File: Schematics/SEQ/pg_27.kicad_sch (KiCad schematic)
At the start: 9 parts, among them U2801 F04, U2802 F169, U2803 F169, U2804 F169, U2805 F169, U2806 F169, U2807 F244, U2808 F244, U2809 F244

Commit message: Much work on SEQ
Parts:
- removed U2803, U2804, U2805, U2806: F169, symbol r1000:F169
- removed U2808, U2809: F244, symbol r1000:F244
- U2802: value F169 -> F169X5; symbol r1000:F169 -> r1000:F169X5; Location K13 -> x99; Name TOP0 -> TOPCNT
- U2807: value F244 -> XBUF20; symbol r1000:F244 -> r1000:XBUF20; Location L13 -> x99; Name RESDRV0A -> TOPDV
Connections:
- net CONTROL_BUS37: now also U2802.5 (D0); no longer U2802.6 (D0)
- net CONTROL_BUS38: now also U2802.7 (D1); no longer U2802.5 (D1)
- net CONTROL_BUS39: now also U2802.9 (D2); no longer U2802.4 (D2)
- net CONTROL_BUS40: now also U2802.11 (D3); no longer U2802.3 (D3)
- net CONTROL_BUS41: now also U2802.13 (D4)
- net CONTROL_BUS42: now also U2802.15 (D5)
- net CONTROL_BUS43: now also U2802.17 (D6)
- net CONTROL_BUS44: now also U2802.19 (D7)
- net CONTROL_BUS45: now also U2802.21 (D8)
- net CONTROL_BUS46: now also U2802.23 (D9)
- net CONTROL_BUS47: now also U2802.25 (D10)
- net CONTROL_BUS48: now also U2802.27 (D11)
- net CONTROL_BUS49: now also U2802.29 (D12)
- net CONTROL_BUS50: now also U2802.31 (D13)
- net CONTROL_BUS51: now also U2802.33 (D14)
- net CONTROL_BUS52: now also U2802.35 (D15)
- net CONTROL_BUS53: now also U2802.37 (D16)
- net CONTROL_BUS54: now also U2802.39 (D17)
- net CONTROL_BUS55: now also U2802.41 (D18)
- net CONTROL_BUS56: now also U2802.43 (D19)
- net OFFSET_BUS37: now also U2807.4 (Y0); no longer U2807.18 (Y0)
- net OFFSET_BUS38: now also U2807.6 (Y1); no longer U2807.16 (Y1)
- net OFFSET_BUS39: now also U2807.8 (Y2); no longer U2807.14 (Y2)
- net OFFSET_BUS40: now also U2807.10 (Y3); no longer U2807.12 (Y3)
- net OFFSET_BUS41: now also U2807.12 (Y4)
- net OFFSET_BUS42: now also U2807.14 (Y5)
- net OFFSET_BUS43: now also U2807.16 (Y6)
- net OFFSET_BUS44: now also U2807.18 (Y7)
- net OFFSET_BUS45: now also U2807.20 (Y8)
- net OFFSET_BUS46: now also U2807.22 (Y9)
- net OFFSET_BUS47: now also U2807.24 (Y10)
- net OFFSET_BUS48: now also U2807.26 (Y11)
- net OFFSET_BUS49: now also U2807.28 (Y12)
- net OFFSET_BUS50: now also U2807.30 (Y13)
- net OFFSET_BUS51: now also U2807.32 (Y14)
- net OFFSET_BUS52: now also U2807.34 (Y15)
- net OFFSET_BUS53: now also U2807.36 (Y16)
- net OFFSET_BUS54: now also U2807.38 (Y17)
- net OFFSET_BUS55: now also U2807.40 (Y18)
- net OFFSET_BUS56: now also U2807.42 (Y19)
- net TOP.CLK~: now also U2802.1 (CLK); no longer U2802.2 (CLK)
- net TOP.EN~: now also U2802.45 (ENP); no longer U2802.7 (ENP)
- net TOP.OE~: now also U2807.2 (OE); no longer U2807.1 (OE0)
- net TOP.U_D~: now also U2802.3 (UP); no longer U2802.1 (UP)
- net TOP37: now also U2802.6 (Q0), U2807.3 (I0); no longer U2802.11 (Q0), U2807.2 (I0)
- net TOP38: now also U2802.8 (Q1), U2807.5 (I1); no longer U2802.12 (Q1), U2807.4 (I1)
- net TOP39: now also U2802.10 (Q2), U2807.7 (I2); no longer U2802.13 (Q2), U2807.6 (I2)
- net TOP40: now also U2802.12 (Q3), U2807.9 (I3); no longer U2802.14 (Q3), U2807.8 (I3)
- net TOP41: now also U2802.14 (Q4), U2807.11 (I4)
- net TOP42: now also U2802.16 (Q5), U2807.13 (I5)
- net TOP43: now also U2802.18 (Q6), U2807.15 (I6)
- net TOP44: now also U2802.20 (Q7), U2807.17 (I7)
- net TOP45: now also U2802.22 (Q8), U2807.19 (I8)
- net TOP46: now also U2802.24 (Q9), U2807.21 (I9)
- net TOP47: now also U2802.26 (Q10), U2807.23 (I10)
- net TOP48: now also U2802.28 (Q11), U2807.25 (I11)
- net TOP49: now also U2802.30 (Q12), U2807.27 (I12)
- net TOP50: now also U2802.32 (Q13), U2807.29 (I13)
- net TOP51: now also U2802.34 (Q14), U2807.31 (I14)
- net TOP52: now also U2802.36 (Q15), U2807.33 (I15)
- net TOP53: now also U2802.38 (Q16), U2807.35 (I16)
- net TOP54: now also U2802.40 (Q17), U2807.37 (I17)
- net TOP55: now also U2802.42 (Q18), U2807.39 (I18)
- net TOP56: now also U2802.44 (Q19), U2807.41 (I19)
- net TOP_LD.RND~: now also U2802.2 (LD); no longer U2802.9 (LD)
- net at U2801.2 (Q): now also U2802.46 (ENT)
- no-connect marks 10 -> 2
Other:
- moved on the sheet: U2801

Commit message: KiCad 6
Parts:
- U2801: value F04 -> (none)
- U2802: value F169X5 -> (none)
- U2807: value XBUF20 -> (none)
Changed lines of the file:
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@@
   (wire (pts (xy 365.76 251.46) (xy 408.94 251.46) ) (stroke (width 0) (type solid) (color 0 0 0 0) ) )
   (global_label "LOCL_STOP.DIAG~" (shape input) (at 114.3 261.62 180) (fields_autoplaced) (effects (font (size 2.54 2.54) ) (justify right) ) (property "Intersheet References" "${INTERSHEET_REFS}" (id 0) (at 77.1797 261.4613 0) (effects (font (size 2.54 2.54) ) (justify right) ) ) )
-  (symbol (lib_id "r1000:F04") (at 139.7 261.62 0) (unit 1) (in_bom yes) (on_board yes) (property "Reference" "U2801" (id 0) (at 139.7 261.62 0) ) (property "Value" "F04" (id 1) (at 140.97 266.7 0) (effects (font (size 2.54 2.54) ) (justify left) ) ) (property "Footprint" "" (id 2) (at 139.7 261.62 0) (effects (font (size 1.27 1.27) ) hide ) ) (property "Datasheet" "" (id 3) (at 139.7 261.62 0) (effects (font (size 1.27 1.27) ) hide ) ) (property "Location" "N39" (id 4) (at 127 266.7 0) (effects (font (size 2.54 2.54) ) (justify left) ) ) (property "Name" "DINV0F" (id 5) (at 139.7 256.54 0) (effects (font (size 2.54 2.54) ) (justify bottom) ) ) (pin "1") (pin "2") )
+  (symbol (lib_id "r1000:F04") (at 139.7 261.62 0) (unit 1) (in_bom yes) (on_board yes) (property "Reference" "U2801" (id 0) (at 139.7 261.62 0) ) (property "Value" "" (id 1) (at 140.97 266.7 0) (effects (font (size 2.54 2.54) ) (justify left) ) ) (property "Footprint" "" (id 2) (at 139.7 261.62 0) (effects (font (size 1.27 1.27) ) hide ) ) (property "Datasheet" "" (id 3) (at 139.7 261.62 0) (effects (font (size 1.27 1.27) ) hide ) ) (property "Location" "N39" (id 4) (at 127 266.7 0) (effects (font (size 2.54 2.54) ) (justify left) ) ) (property "Name" "DINV0F" (id 5) (at 139.7 256.54 0) (effects (font (size 2.54 2.54) ) (justify bottom) ) ) (pin "1") (pin "2") )
   (global_label "CONTROL_BUS[37..56]" (shape input) (at 157.48 147.32 180) (fields_autoplaced) (effects (font (size 2.54 2.54) ) (justify right) ) (property "Intersheet References" "${INTERSHEET_REFS}" (id 0) (at 110.5626 147.1613 0) (effects (font (size 2.54 2.54) ) (justify right) ) ) )
   (bus_entry (at 162.56 152.4) (size 2.54 2.54) (stroke (width 0) (type solid) (color 0 0 0 0) ) )
@@
   (global_label "TOP_LD.RND~" (shape input) (at 213.36 121.92 180) (fields_autoplaced) (effects (font (size 2.54 2.54) ) (justify right) ) (property "Intersheet References" "${INTERSHEET_REFS}" (id 0) (at 184.1016 121.7613 0) (effects (font (size 2.54 2.54) ) (justify right) ) ) )
   (global_label "TOP.CLK~" (shape input) (at 213.36 129.54 180) (fields_autoplaced) (effects (font (size 2.54 2.54) ) (justify right) ) (property "Intersheet References" "${INTERSHEET_REFS}" (id 0) (at 191.2378 129.3813 0) (effects (font (size 2.54 2.54) ) (justify right) ) ) )
-  (symbol (lib_id "r1000:F169X5") (at 226.06 261.62 0) (unit 1) (in_bom yes) (on_board yes) (property "Reference" "U2802" (id 0) (at 228.6 256.54 0) ) (property "Value" "F169X5" (id 1) (at 224.79 266.7 0) (effects (font (size 2.54 2.54) ) (justify left) ) ) (property "Footprint" "" (id 2) (at 227.33 262.89 0) (effects (font (size 1.27 1.27) ) hide ) ) (property "Datasheet" "" (id 3) (at 227.33 262.89 0) (effects (font (size 1.27 1.27) ) hide ) ) (property "Location" "x99" (id 4) (at 224.79 261.62 0) (effects (font (size 2.54 2.54) ) (justify left) ) ) (property "Name" "TOPCNT" (id 5) (at 229.87 274.32 0) (effects (font (size 2.54 2.54) ) (justify bottom) ) ) (pin "1") (pin "10") (pin "11") (pin "12") (pin "13") (pin "14") (pin "15") (pin "16") (pin "17") (pin "18") (pin "19") (pin "2") (pin "20") (pin "21") (pin "22") (pin "23") (pin "24") (pin "25") (pin "26") (pin "27") (pin "28") (pin "29") (pin "3") (pin "30") (pin "31") (pin "32") (pin "33") (pin "34") (pin "35") (pin "36") (pin "37") (pin "38") (pin "39") (pin "4") (pin "40") (pin "41") (pin "42") (pin "43") (pin "44") (pin "45") (pin "46") (pin "5") (pin "6") (pin "7") (pin "8") (pin "9") )
+  (symbol (lib_id "r1000:F169X5") (at 226.06 261.62 0) (unit 1) (in_bom yes) (on_board yes) (property "Reference" "U2802" (id 0) (at 228.6 256.54 0) ) (property "Value" "" (id 1) (at 224.79 266.7 0) (effects (font (size 2.54 2.54) ) (justify left) ) ) (property "Footprint" "" (id 2) (at 227.33 262.89 0) (effects (font (size 1.27 1.27) ) hide ) ) (property "Datasheet" "" (id 3) (at 227.33 262.89 0) (effects (font (size 1.27 1.27) ) hide ) ) (property "Location" "x99" (id 4) (at 224.79 261.62 0) (effects (font (size 2.54 2.54) ) (justify left) ) ) (property "Name" "TOPCNT" (id 5) (at 229.87 274.32 0) (effects (font (size 2.54 2.54) ) (justify bottom) ) ) (pin "1") (pin "10") (pin "11") (pin "12") (pin "13") (pin "14") (pin "15") (pin "16") (pin "17") (pin "18") (pin "19") (pin "2") (pin "20") (pin "21") (pin "22") (pin "23") (pin "24") (pin "25") (pin "26") (pin "27") (pin "28") (pin "29") (pin "3") (pin "30") (pin "31") (pin "32") (pin "33") (pin "34") (pin "35") (pin "36") (pin "37") (pin "38") (pin "39") (pin "4") (pin "40") (pin "41") (pin "42") (pin "43") (pin "44") (pin "45") (pin "46") (pin "5") (pin "6") (pin "7") (pin "8") (pin "9") )
   (no_connect (at 248.92 149.86) )
   (label "TOP37" (at 256.54 154.94 0) (effects (font (size 2.54 2.54) ) (justify left bottom) ) )
@@
   (no_connect (at 342.9 139.7) )
   (global_label "TOP.OE~" (shape input) (at 345.44 132.08 180) (fields_autoplaced) (effects (font (size 2.54 2.54) ) (justify right) ) (property "Intersheet References" "${INTERSHEET_REFS}" (id 0) (at 325.495 131.9213 0) (effects (font (size 2.54 2.54) ) (justify right) ) ) )
-  (symbol (lib_id "r1000:XBUF20") (at 345.44 248.92 0) (unit 1) (in_bom yes) (on_board yes) (property "Reference" "U2807" (id 0) (at 347.98 243.84 0) ) (property "Value" "XBUF20" (id 1) (at 341.63 254 0) (effects (font (size 2.54 2.54) ) (justify left) ) ) (property "Footprint" "" (id 2) (at 346.71 250.19 0) (effects (font (size 1.27 1.27) ) hide ) ) (property "Datasheet" "" (id 3) (at 346.71 250.19 0) (effects (font (size 1.27 1.27) ) hide ) ) (property "Location" "x99" (id 4) (at 344.17 248.92 0) (effects (font (size 2.54 2.54) ) (justify left) ) ) (property "Name" "TOPDV" (id 5) (at 349.25 261.62 0) (effects (font (size 2.54 2.54) ) (justify bottom) ) ) (pin "1") (pin "10") (pin "11") (pin "12") (pin "13") (pin "14") (pin "15") (pin "16") (pin "17") (pin "18") (pin "19") (pin "2") (pin "20") (pin "21") (pin "22") (pin "23") (pin "24") (pin "25") (pin "26") (pin "27") (pin "28") (pin "29") (pin "3") (pin "30") (pin "31") (pin "32") (pin "33") (pin "34") (pin "35") (pin "36") (pin "37") (pin "38") (pin "39") (pin "4") (pin "40") (pin "41") (pin "42") (pin "5") (pin "6") (pin "7") (pin "8") (pin "9") )
+  (symbol (lib_id "r1000:XBUF20") (at 345.44 248.92 0) (unit 1) (in_bom yes) (on_board yes) (property "Reference" "U2807" (id 0) (at 347.98 243.84 0) ) (property "Value" "" (id 1) (at 341.63 254 0) (effects (font (size 2.54 2.54) ) (justify left) ) ) (property "Footprint" "" (id 2) (at 346.71 250.19 0) (effects (font (size 1.27 1.27) ) hide ) ) (property "Datasheet" "" (id 3) (at 346.71 250.19 0) (effects (font (size 1.27 1.27) ) hide ) ) (property "Location" "x99" (id 4) (at 344.17 248.92 0) (effects (font (size 2.54 2.54) ) (justify left) ) ) (property "Name" "TOPDV" (id 5) (at 349.25 261.62 0) (effects (font (size 2.54 2.54) ) (justify bottom) ) ) (pin "1") (pin "10") (pin "11") (pin "12") (pin "13") (pin "14") (pin "15") (pin "16") (pin "17") (pin "18") (pin "19") (pin "2") (pin "20") (pin "21") (pin "22") (pin "23") (pin "24") (pin "25") (pin "26") (pin "27") (pin "28") (pin "29") (pin "3") (pin "30") (pin "31") (pin "32") (pin "33") (pin "34") (pin "35") (pin "36") (pin "37") (pin "38") (pin "39") (pin "4") (pin "40") (pin "41") (pin "42") (pin "5") (pin "6") (pin "7") (pin "8") (pin "9") )
   (label "OFFSET_BUS37" (at 375.92 154.94 0) (effects (font (size 2.54 2.54) ) (justify left bottom) ) )
   (label "OFFSET_BUS38" (at 375.92 160.02 0) (effects (font (size 2.54 2.54) ) (justify left bottom) ) )

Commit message: Recover from KiCad-6 munging
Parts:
- U2801: value (none) -> F04
- U2802: value (none) -> F169X5
- U2807: value (none) -> XBUF20

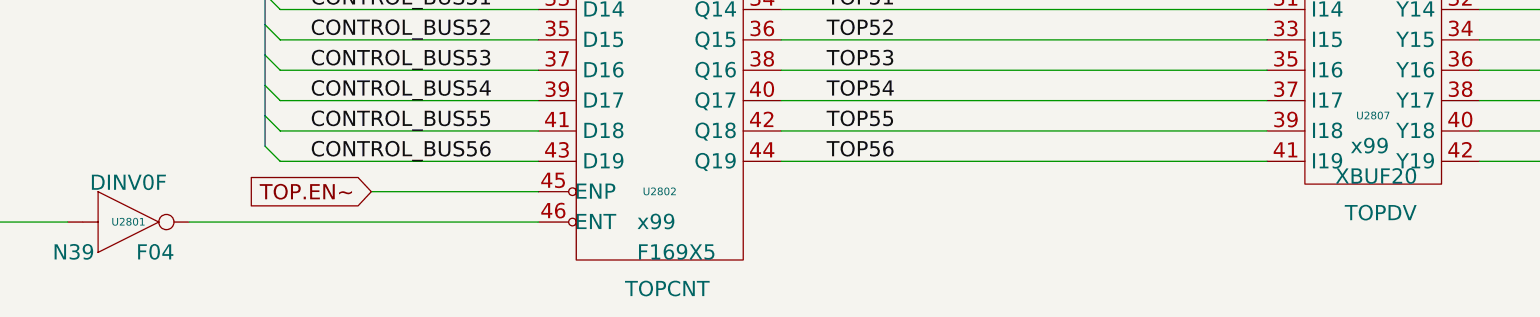
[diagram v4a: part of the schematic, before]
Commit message: Fix polarity of unused part of driven FIU bus.
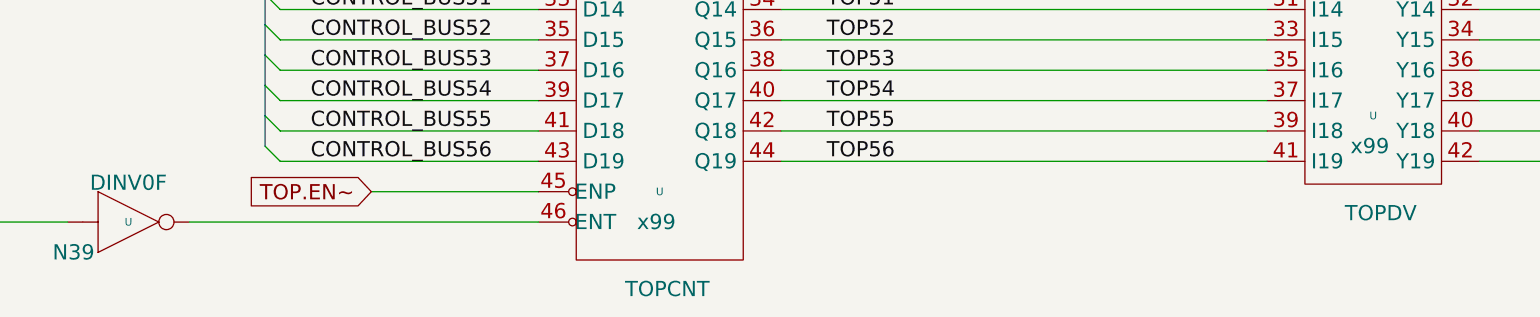
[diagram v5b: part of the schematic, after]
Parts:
- removed U2801: F04, symbol r1000:F04
- removed U2802: F169X5, symbol r1000:F169X5
- removed U2807: XBUF20, symbol r1000:XBUF20
- added U: (no value), symbol r1000:F169X5
- added U: (no value), symbol r1000:F04
- added U: (no value), symbol r1000:XBUF20
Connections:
- net CONTROL_BUS37: now also U.5 (D0)
- net CONTROL_BUS38: now also U.7 (D1)
- net CONTROL_BUS39: now also U.9 (D2)
- net CONTROL_BUS40: now also U.11 (D3)
- net CONTROL_BUS41: now also U.13 (D4)
- net CONTROL_BUS42: now also U.15 (D5)
- net CONTROL_BUS43: now also U.17 (D6)
- net CONTROL_BUS44: now also U.19 (D7)
- net CONTROL_BUS45: now also U.21 (D8)
- net CONTROL_BUS46: now also U.23 (D9)
- net CONTROL_BUS47: now also U.25 (D10)
- net CONTROL_BUS48: now also U.27 (D11)
- net CONTROL_BUS49: now also U.29 (D12)
- net CONTROL_BUS50: now also U.31 (D13)
- net CONTROL_BUS51: now also U.33 (D14)
- net CONTROL_BUS52: now also U.35 (D15)
- net CONTROL_BUS53: now also U.37 (D16)
- net CONTROL_BUS54: now also U.39 (D17)
- net CONTROL_BUS55: now also U.41 (D18)
- net CONTROL_BUS56: now also U.43 (D19)
- net LOCL_STOP.DIAG~: now also U.1 (D0)
- net OFFSET_BUS37: now also U.4 (Y0)
- net OFFSET_BUS38: now also U.6 (Y1)
- net OFFSET_BUS39: now also U.8 (Y2)
- net OFFSET_BUS40: now also U.10 (Y3)
- net OFFSET_BUS41: now also U.12 (Y4)
- net OFFSET_BUS42: now also U.14 (Y5)
- net OFFSET_BUS43: now also U.16 (Y6)
- net OFFSET_BUS44: now also U.18 (Y7)
- net OFFSET_BUS45: now also U.20 (Y8)
- net OFFSET_BUS46: now also U.22 (Y9)
- net OFFSET_BUS47: now also U.24 (Y10)
- net OFFSET_BUS48: now also U.26 (Y11)
- net OFFSET_BUS49: now also U.28 (Y12)
- net OFFSET_BUS50: now also U.30 (Y13)
- net OFFSET_BUS51: now also U.32 (Y14)
- net OFFSET_BUS52: now also U.34 (Y15)
- net OFFSET_BUS53: now also U.36 (Y16)
- net OFFSET_BUS54: now also U.38 (Y17)
- net OFFSET_BUS55: now also U.40 (Y18)
- net OFFSET_BUS56: now also U.42 (Y19)
- net TOP.CLK~: now also U.1 (CLK)
- net TOP.EN~: now also U.45 (ENP)
- net TOP.OE~: now also U.2 (OE)
- net TOP.U_D~: now also U.3 (UP)
- net TOP37: now also U.3 (I0), U.6 (Q0)
- net TOP38: now also U.5 (I1), U.8 (Q1)
- net TOP39: now also U.10 (Q2), U.7 (I2)
- net TOP40: now also U.12 (Q3), U.9 (I3)
- net TOP41: now also U.11 (I4), U.14 (Q4)
- net TOP42: now also U.13 (I5), U.16 (Q5)
- net TOP43: now also U.15 (I6), U.18 (Q6)
- net TOP44: now also U.17 (I7), U.20 (Q7)
- net TOP45: now also U.19 (I8), U.22 (Q8)
- net TOP46: now also U.21 (I9), U.24 (Q9)
- net TOP47: now also U.23 (I10), U.26 (Q10)
- net TOP48: now also U.25 (I11), U.28 (Q11)
- net TOP49: now also U.27 (I12), U.30 (Q12)
- net TOP50: now also U.29 (I13), U.32 (Q13)
- net TOP51: now also U.31 (I14), U.34 (Q14)
- net TOP52: now also U.33 (I15), U.36 (Q15)
- net TOP53: now also U.35 (I16), U.38 (Q16)
- net TOP54: now also U.37 (I17), U.40 (Q17)
- net TOP55: now also U.39 (I18), U.42 (Q18)
- net TOP56: now also U.41 (I19), U.44 (Q19)
- net TOP_LD.RND~: now also U.2 (LD)
- new net: U.2 (Q), U.46 (ENT)
